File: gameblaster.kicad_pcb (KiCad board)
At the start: 2 copper layers, 136.7 x 109.8 mm, 72 parts, among them IC1 TEA2025, IC10 74LS138, IC11 74LS08, IC12 74LS14, IC2 SAA1099, IC3 SAA1099, IC4 74LS374, IC5 74LS138, IC6 74LS74, IC7 74LS245, IC8 74LS32, IC9 74LS125, J1 Conn_02x06_Odd_Even

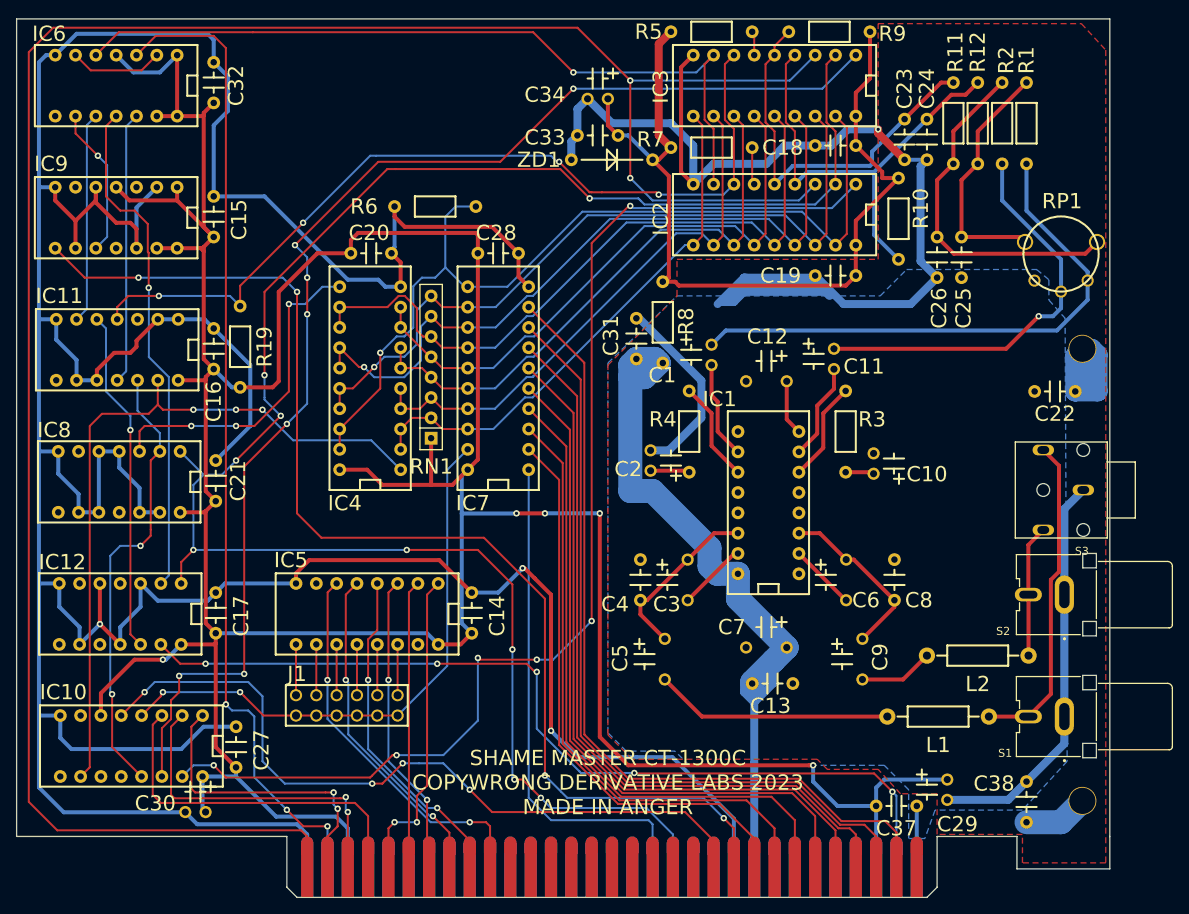
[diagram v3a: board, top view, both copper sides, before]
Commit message: add logo, engorge zones, clip solder mask from card fingers
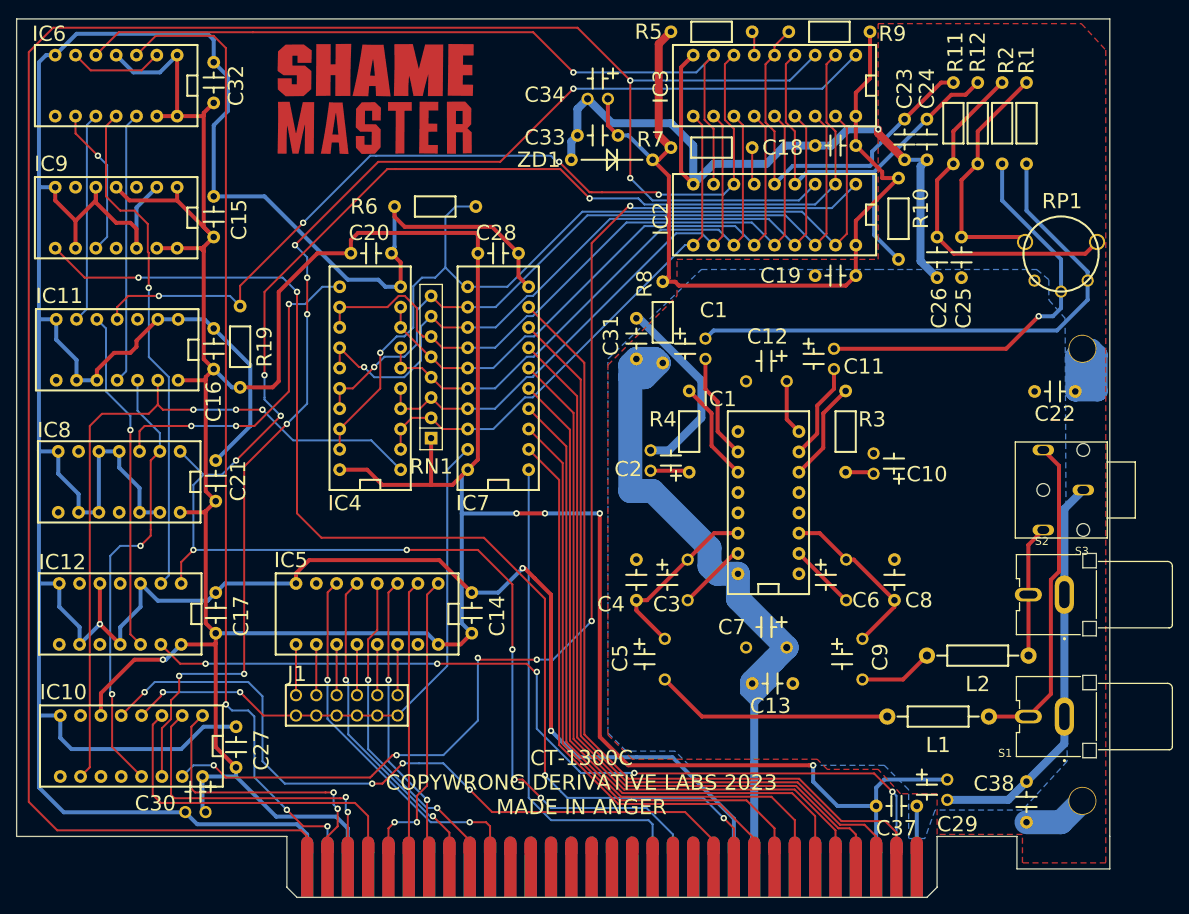
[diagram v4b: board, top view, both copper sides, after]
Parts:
- S2: footprint gameblaster:CUI_RCJ-042 -> gameblaster:CUI_RCJ-043
- moved C1 1.08 mm to (146.8, 68.6)
- moved C4 0.51 mm to (138.2, 101.3)
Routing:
- net /AGND: track 241.1 -> 170.7 mm
- net Net-(C1-Pad2): track 12.2 -> 13.3 mm
- net Net-(C3-Pad1): track 21.8 -> 22.5 mm
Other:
- board text added: "CT-1300C COPYWRONG DERIVATIVE LABS 2023 MADE IN ANGER"
- board text removed: "SHAME MASTER CT-1300C COPYWRONG DERIVATIVE LABS 2023 MADE IN ANGER"

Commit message: so much dumb shit
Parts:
- removed C24: 680pF, gameblaster:CAPAC200
- removed IC12: 74LS14, gameblaster:DIP254P762X635-14
- removed R10: 1K, gameblaster:RESA400
- added C35: 0.1uF?, gameblaster:CAPAC200, F.Cu at (88.4, 80.8)
- C10, C2: value 47uF 16V -> 22uF 16V
- C17: value 0.1uF -> 1uF tant; footprint gameblaster:CAPAC200 -> gameblaster:CAPAP100
- C23: value 680pF -> 1uF tant; footprint gameblaster:CAPAC200 -> gameblaster:CAPAP100
- R6: value 4.7K -> 1K
- R8: value 10K -> 470R
- R9: value 1K -> 10K
- moved C17 106.2 mm to (174.8, 42.7), turned to 90 degrees
- moved R9 82.0 mm to (91.9, 62.5), turned to 90 degrees
- moved C33 12.8 mm to (132.8, 55.6), turned to 90 degrees
- moved C21 12.4 mm to (85.6, 96.3)
- moved IC8 12.4 mm to (81.2, 95.1)
- moved R19 12.2 mm to (88.6, 62.5)
- moved ZD1 11.5 mm to (136.2, 57.0), turned to 90 degrees
- moved C16 8.38 mm to (85.3, 75.7)
- moved IC11 8.25 mm to (80.9, 74.4)
- moved IC9 4.13 mm to (80.8, 53.8)
- moved C15 4.06 mm to (85.3, 54.9)
- moved C34 3.90 mm to (133.4, 42.3)
- moved R1 2.57 mm to (189.4, 35.7)
- moved R2 2.57 mm to (186.3, 35.7)
- moved R11 2.57 mm to (180.2, 35.7)
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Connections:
- net /ADDR_RANGE renamed /~{ADDR_RANGE}
- net /IOR renamed /~{IOR}
- net /REG_CLOCK renamed /~{REG_CLOCK}
- BUS1 pad 13: /IOW -> /~{IOW}
- C1 pad 1: /RIGHT_IN -> Net-(C1-Pad1)
- C1 pad 2: Net-(C1-Pad2) -> /RIGHT_IN
- C11 pad 1: /LEFT_IN -> Net-(C11-Pad1)
- C11 pad 2: Net-(C11-Pad2) -> /LEFT_IN
- C13 pad 1: /+12V -> /+5VA
- C17 pad 1: /GND -> Net-(C26-Pad1)
- C17 pad 2: /VCC -> Net-(R2-Pad1)
- C18 pad 2: /+5VD -> /+5VA
- C19 pad 1: /+5VD -> /+5VA
- C23 pad 1: /LEFT_RAW -> Net-(C25-Pad1)
- C23 pad 2: /AGND -> Net-(R1-Pad1)
- C33 pad 1: /+5VD -> /+5VA
- C34 pad 1: /+5VD -> /+5VA
- C37 pad 2: /VCC -> /ISA_RST
- C7 pad 1: /+12V -> /+5VA
- IC1 pad 10: Net-(C1-Pad2) -> Net-(C1-Pad1)
- IC1 pad 16: /+12V -> /+5VA
- IC1 pad 7: Net-(C11-Pad2) -> Net-(C11-Pad1)
- IC10 pad 10: /2xA_2xB -> /~{2xA_2xB}
- IC10 pad 12: unconnected-(IC10-Pad12) -> /~{2x6_2x7}
- IC10 pad 13: /2x6_2x7 -> /~{7FH_READ}
- IC10 pad 14: /2x2_2x3 -> /~{2x2_2x3}
- IC10 pad 15: /2x0_2x1 -> /~{2x0_2x1}
- IC11 pad 1: /GND -> /VCC
- IC11 pad 12: /2x6_2x7 -> /~{2x0_2x1}
- IC11 pad 13: /2xA_2xB -> /~{2x2_2x3}
- IC11 pad 2: /GND -> /~{IOW}
- IC11 pad 3: unconnected-(IC11-Pad3) -> /~{SAA_IOW}
- IC11 pad 4: /~{DTACK} -> unconnected-(IC11-Pad4)
- IC11 pad 5: /~{RESET} -> unconnected-(IC11-Pad5)
- IC11 pad 6: Net-(IC11-Pad6) -> unconnected-(IC11-Pad6)
- IC2 pad 1: /2x0_2x1 -> /~{SAA_IOW}
- IC2 pad 18: /+5VD -> /+5VA
- IC2 pad 2: /IOW -> /~{2x0_2x1}
- IC3 pad 1: /2x2_2x3 -> /~{SAA_IOW}
- IC3 pad 18: /+5VD -> /+5VA
- IC3 pad 2: /IOW -> /~{2x2_2x3}
- IC4 pad 1: /2xA_2xB -> /~{2xA_2xB}
- IC6 pad 10: Net-(IC11-Pad6) -> Net-(IC9-Pad6)
- IC6 pad 11: Net-(IC12-Pad2) -> Net-(IC9-Pad3)
- IC8 pad 1: /IOW -> /~{IOW}
- IC8 pad 2: /2x6_2x7 -> /~{2x6_2x7}
- IC9 pad 1: /VCC -> /~{IOW}
- IC9 pad 2: /GND -> /VCC
- IC9 pad 3: unconnected-(IC9-Pad3) -> Net-(IC9-Pad3)
- IC9 pad 4: /VCC -> /ISA_RST
- IC9 pad 5: /GND -> /~{DTACK}
- IC9 pad 6: unconnected-(IC9-Pad6) -> Net-(IC9-Pad6)
- R1 pad 1: Net-(C25-Pad1) -> Net-(R1-Pad1)
- R2 pad 1: Net-(C26-Pad1) -> Net-(R2-Pad1)
- R5 pad 1: /+5VD -> /+5VA
- R7 pad 1: /+5VD -> /+5VA
- R8 pad 2: /+5VD -> /+5VA
- R9 pad 1: /+5VD -> Net-(IC9-Pad3)
- R9 pad 2: /LEFT_RAW -> /GND
- RP1 pad 2A: Net-(C26-Pad1) -> /LEFT_IN
- RP1 pad 2B: Net-(C25-Pad1) -> /RIGHT_IN
- RP1 pad 3A: /LEFT_IN -> Net-(R2-Pad1)
- RP1 pad 3B: /RIGHT_IN -> Net-(R1-Pad1)
- ZD1 pad 1: /+5VD -> /+5VA
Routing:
- net /GND: track 541.0 -> 0.00 mm, vias 3 -> 0
- net /VCC: track 452.3 -> 0.00 mm, vias 5 -> 0
- net /ISA_A00: track 275.4 -> 0.00 mm, vias 2 -> 0
- net /IOW: track 238.8 -> 0.00 mm, vias 9 -> 0
- net /AGND: track 170.7 -> 0.00 mm, vias 1 -> 0
- net /2x2_2x3: track 159.1 -> 0.00 mm, vias 7 -> 0
- net /2x0_2x1: track 148.8 -> 0.00 mm, vias 6 -> 0
- net /~{IOW}: track 0.00 -> 143.4 mm, vias 0 -> 5
- net /+5VD: track 107.6 -> 0.00 mm
- net /ISA_RST: track 113.2 -> 217.1 mm, vias 5 -> 3
- net /+12V: track 93.9 -> 0.00 mm
- net /2xA_2xB: track 90.7 -> 0.00 mm, vias 3 -> 0
- net /~{2xA_2xB}: track 0.00 -> 78.2 mm, vias 0 -> 4
- net /~{DTACK}: track 108.6 -> 36.9 mm, vias 4 -> 1
- net /RIGHT_IN: track 69.9 -> 0.00 mm
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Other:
- board text added: "210"
- board text added: "220"
- board text added: "230"
- board text added: "240"
- board text added: "250"
- board text added: "260"
- board text added: "JLCJLCJLCJLC"
- board text added: "Special Thanks: TubeTime - reverse engineering of the big stupid DIP-40; DTACK circuit and TEA2025B section from the Snark Barker; copious footprints and silkscreen Tronix - original transceiver/register logic for card detection leadedsolder - generally being a shithead and encouraging my terrible ideas"
- board text removed: "Special Thanks: TubeTime - reverse engineering of the big stupid DIP-40; DTACK circuit and TEA2025B section from the Snark Barker; copious footprints and silkscreen Tronix - original transceiver/register logic for card detection seat safety switch - generally being a shithead and encouraging my terrible ideas"

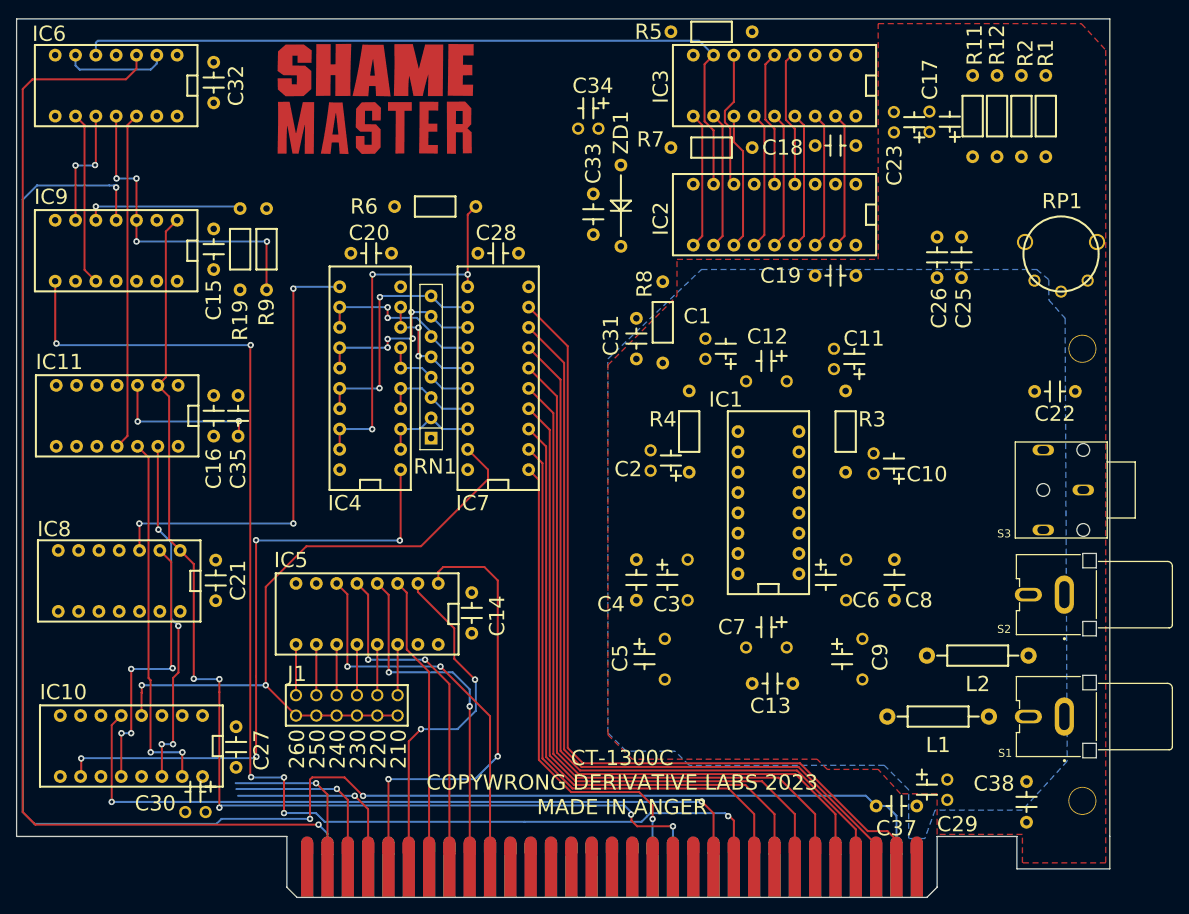
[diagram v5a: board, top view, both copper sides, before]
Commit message: Separate +5VA and VDDA; re-add SAA1099 output current source; use power symbols
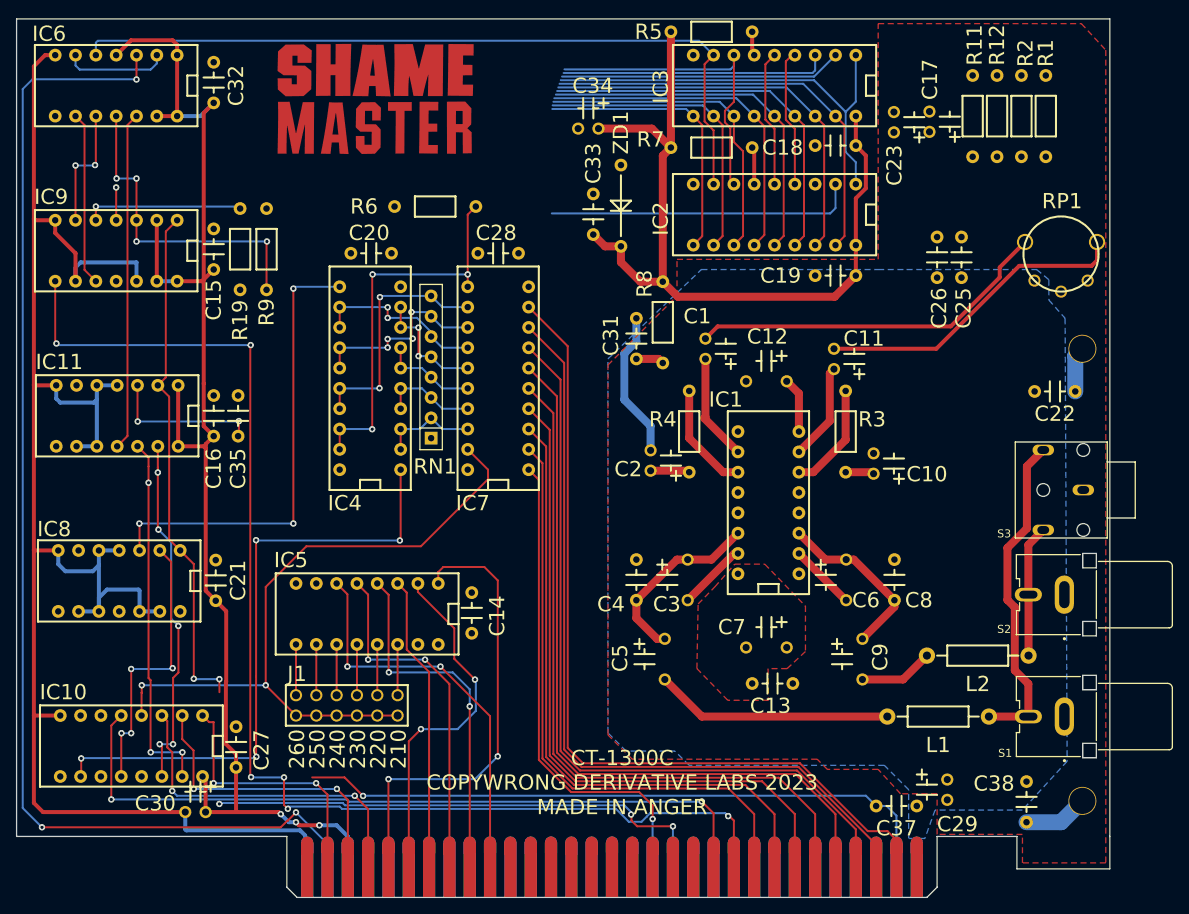
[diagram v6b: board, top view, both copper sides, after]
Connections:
- net /ISA_IO_CH_RDY renamed /~{IORDY}
- C38 pad 1: /AGND -> /CHASSIS
- C38 pad 2: /CHASSIS -> /AGND
- IC11 pad 4: unconnected-(IC11-Pad4) -> /GND
- IC11 pad 5: unconnected-(IC11-Pad5) -> /GND
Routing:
- net /GND: track 0.00 -> 221.5 mm
- net /VCC: track 0.00 -> 171.5 mm, vias 0 -> 3
- net /ISA_RST: track 217.1 -> 85.9 mm, vias 3 -> 2
- net /+5VA: track 0.00 -> 101.0 mm
- net /~{SAA_IOW}: track 19.1 -> 73.6 mm
- net /RIGHT_IN: track 0.00 -> 45.7 mm
- net Net-(L1-Pad1): track 0.00 -> 41.2 mm
- net /LEFT_IN: track 0.00 -> 39.8 mm
- net /~{2x0_2x1}: track 45.9 -> 84.7 mm, vias 2 -> 3
- net /DB7: track 65.4 -> 101.6 mm
- net /~{2x2_2x3}: track 44.1 -> 79.7 mm, vias 4 -> 5
- net /DB6: track 47.6 -> 81.2 mm
- net /ISA_A00: track 0.00 -> 33.5 mm
- net /DB5: track 41.1 -> 72.1 mm
- net Net-(C5-Pad2): track 0.00 -> 29.7 mm
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- added copper zone on F.Cu, net /+5VA

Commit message: updated board
yes i know the left ICs are misaligned
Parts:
- added C24: 680pF, gameblaster:CAPAC200, F.Cu at (170.6, 42.7)
- added C36: 680pF, gameblaster:CAPAC200, F.Cu at (173.4, 42.7)
- added R10: 1.5K, gameblaster:RESA400, F.Cu at (172.7, 40.4)
- added R13: 1.5K, gameblaster:RESA400, F.Cu at (165.4, 30.2)
- C1, C11: value 10uF 16V -> 0.22uF 16V
- moved R2 7.75 mm to (194.1, 35.7)
- moved R11 7.11 mm to (187.3, 35.7)
- moved C17 6.35 mm to (181.0, 41.5)
- moved C23 6.24 mm to (176.5, 41.5)
- moved C31 5.08 mm to (138.2, 66.0), turned to -90 degrees
- moved C25 3.56 mm to (175.3, 55.9)
- moved C19 3.43 mm to (169.0, 60.7)
- moved C26 3.18 mm to (178.9, 55.9)
- moved R1 1.27 mm to (190.6, 35.7)
- moved R12 0.76 mm to (184.0, 35.7)
- moved R6 0.25 mm to (118.1, 52.3)
- renumbered IC9 to IC10, IC6 to IC11, IC7 to IC4, IC4 to IC5, IC5 to IC6, IC10 to IC7, IC11 to IC9
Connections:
- net /+12V renamed +12V
- BUS1 pad 1: /GND -> GNDREF
- BUS1 pad 10: /GND -> unconnected-(BUS1-Pad10)
- BUS1 pad 29: /VCC -> VCC
- BUS1 pad 3: /VCC -> +5VA
- BUS1 pad 31: /GND -> GND
- C10 pad 2: /AGND -> GNDREF
- C12 pad 2: /AGND -> GNDREF
- C13 pad 1: /+5VA -> +5VA
- C13 pad 2: /AGND -> GNDREF
- C14 pad 1: /GND -> GND
- C14 pad 2: /VCC -> VCC
- C15 pad 1: /GND -> GND
- C15 pad 2: /VCC -> VCC
- C16 pad 1: /GND -> GND
- C16 pad 2: /VCC -> VCC
- C18 pad 1: /AGND -> GNDREF
- C18 pad 2: /+5VA -> +5VA
- C19 pad 1: /+5VA -> GNDREF
- C19 pad 2: /AGND -> +5VA
- C2 pad 2: /AGND -> GNDREF
- C20 pad 1: /GND -> GND
- C20 pad 2: /VCC -> VCC
- C21 pad 1: /GND -> GND
- C21 pad 2: /VCC -> VCC
- C22 pad 1: /AGND -> GNDREF
- C25 pad 2: /AGND -> GNDREF
- C26 pad 2: /AGND -> GNDREF
- C27 pad 1: /GND -> GND
- C27 pad 2: /VCC -> VCC
- C28 pad 1: /VCC -> VCC
- C28 pad 2: /GND -> GND
- C29 pad 1: /VCC -> +5VA
- C29 pad 2: /AGND -> GNDREF
- C30 pad 1: /VCC -> VCC
- C30 pad 2: /GND -> GND
- C31 pad 2: /AGND -> GNDREF
- C32 pad 1: /GND -> GND
- C32 pad 2: /VCC -> VCC
- C33 pad 1: /+5VA -> VDDA
- C33 pad 2: /AGND -> GNDREF
- C34 pad 1: /+5VA -> VDDA
- C34 pad 2: /AGND -> GNDREF
- C35 pad 2: /GND -> GND
- C37 pad 1: /GND -> GNDREF
- C38 pad 1: /CHASSIS -> GNDREF
- C38 pad 2: /AGND -> /CHASSIS
- C4 pad 1: Net-(C3-Pad1) -> GNDREF
- C4 pad 2: /AGND -> Net-(C3-Pad1)
- C7 pad 1: /+5VA -> +5VA
- C7 pad 2: /AGND -> GNDREF
- C8 pad 2: /AGND -> GNDREF
- IC1 pad 12: /AGND -> GNDREF
- IC1 pad 13: /AGND -> GNDREF
- IC1 pad 16: /+5VA -> +5VA
- IC1 pad 4: /AGND -> GNDREF
- IC1 pad 5: /AGND -> GNDREF
- IC1 pad 9: /AGND -> GNDREF
- IC10 pad 12: /GND -> GND
- IC10 pad 13: /VCC -> VCC
- IC10 pad 14: /VCC -> VCC
- IC10 pad 2: /VCC -> VCC
- IC10 pad 7: /GND -> GND
- IC10 pad 9: /GND -> GND
- IC11 pad 1: /VCC -> VCC
- IC11 pad 13: /VCC -> VCC
- IC11 pad 14: /VCC -> VCC
- IC11 pad 4: /VCC -> VCC
- IC11 pad 7: /GND -> GND
- IC2 pad 18: /+5VA -> +5VA
- IC2 pad 9: /AGND -> GNDREF
- IC3 pad 18: /+5VA -> +5VA
- IC3 pad 9: /AGND -> GNDREF
- IC4 pad 10: /GND -> GND
- IC4 pad 20: /VCC -> VCC
- IC5 pad 10: /GND -> GND
- IC5 pad 20: /VCC -> VCC
- IC6 pad 16: /VCC -> VCC
- IC6 pad 8: /GND -> GND
- IC7 pad 16: /VCC -> VCC
- IC7 pad 6: /VCC -> VCC
- IC7 pad 8: /GND -> GND
- IC8 pad 10: /GND -> GND
- IC8 pad 12: /GND -> GND
- IC8 pad 13: /GND -> GND
- IC8 pad 14: /VCC -> VCC
- IC8 pad 4: /GND -> GND
- IC8 pad 5: /GND -> GND
- IC8 pad 7: /GND -> GND
- IC8 pad 9: /GND -> GND
- IC9 pad 1: /VCC -> VCC
- IC9 pad 10: /GND -> GND
- IC9 pad 14: /VCC -> VCC
- IC9 pad 4: /GND -> GND
- IC9 pad 5: /GND -> GND
- IC9 pad 7: /GND -> GND
- IC9 pad 9: /GND -> GND
- R19 pad 1: /VCC -> VCC
- R5 pad 1: /+5VA -> VDDA
- R6 pad 2: /GND -> GND
- R7 pad 1: /+5VA -> VDDA
- R8 pad 2: /+5VA -> VDDA
- R9 pad 2: /GND -> GND
- RN1 pad 1: /VCC -> VCC
- RP1 pad 1: /AGND -> GNDREF
- S1 pad 1: /AGND -> GNDREF
- S2 pad 1: /AGND -> GNDREF
- S3 pad 1: /AGND -> GNDREF
- ZD1 pad 1: /+5VA -> VDDA
- ZD1 pad 2: /AGND -> GNDREF
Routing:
- net GND: track 0.00 -> 413.0 mm, vias 0 -> 10
- net VCC: track 0.00 -> 308.8 mm, vias 0 -> 7
- net /GND: track 221.5 -> 0.00 mm
- net /ISA_A00: track 33.5 -> 254.4 mm
- net /VCC: track 171.5 -> 0.00 mm, vias 3 -> 0
- net +5VA: track 0.00 -> 113.1 mm, vias 0 -> 1
- net /+5VA: track 101.0 -> 0.00 mm
- net /~{2x2_2x3}: track 79.7 -> 175.2 mm, vias 5 -> 9
- net GNDREF: track 0.00 -> 93.8 mm
- net /ISA_RST: track 85.9 -> 177.5 mm, vias 2 -> 5
- net +12V: track 3.51 -> 92.8 mm
- net /~{2x0_2x1}: track 84.7 -> 171.1 mm, vias 3 -> 8
- net VDDA: track 0.00 -> 86.3 mm
- net /~{SAA_IOW}: track 73.6 -> 154.3 mm, vias 2 -> 5
- net /~{DTACK}: track 59.6 -> 113.8 mm
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- added copper zone on F.Cu, net +5VA
- added copper zone on B.Cu, net GNDREF
- added copper zone on F.Cu, net GNDREF
- removed copper zone on F.Cu, net /+5VA
- removed copper zone on B.Cu, net /AGND
- removed copper zone on F.Cu, net /AGND

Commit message: realign IC7 through IC11
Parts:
- moved IC10 0.38 mm to (81.2, 53.8)
- moved IC12 0.38 mm to (81.2, 33.1)
- moved IC7 0.25 mm to (83.7, 115.7)
- moved IC9 0.25 mm to (81.2, 74.4)
- renumbered IC11 to IC12
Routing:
- net +5VA: track 113.1 -> 292.0 mm
- net Net-(C3-Pad1): track 23.0 -> 25.4 mm
- net VCC: track 308.8 -> 307.1 mm
- net Net-(C25-Pad1): track 23.0 -> 21.9 mm
- net Net-(IC12-Pad2): track 16.5 -> 17.3 mm
- net /RIGHT_IN: track 58.6 -> 57.9 mm
- net /SAA_CLK: track 96.7 -> 96.1 mm
- net /~{2x0_2x1}: track 171.1 -> 170.9 mm, vias 8 -> 7
- net /~{2x6_2x7}: track 35.3 -> 35.0 mm, vias 4 -> 2
- net /~{2x2_2x3}: track 175.2 -> 175.1 mm, vias 9 -> 7
- removed copper zone on F.Cu, net +5VA
